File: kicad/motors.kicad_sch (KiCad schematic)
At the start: 33 parts, among them U1 DRV8251A, U15 DRV8251A, U16 DRV8251A, U17 DRV8251A, U2 DRV8251A, U3 DRV8251A

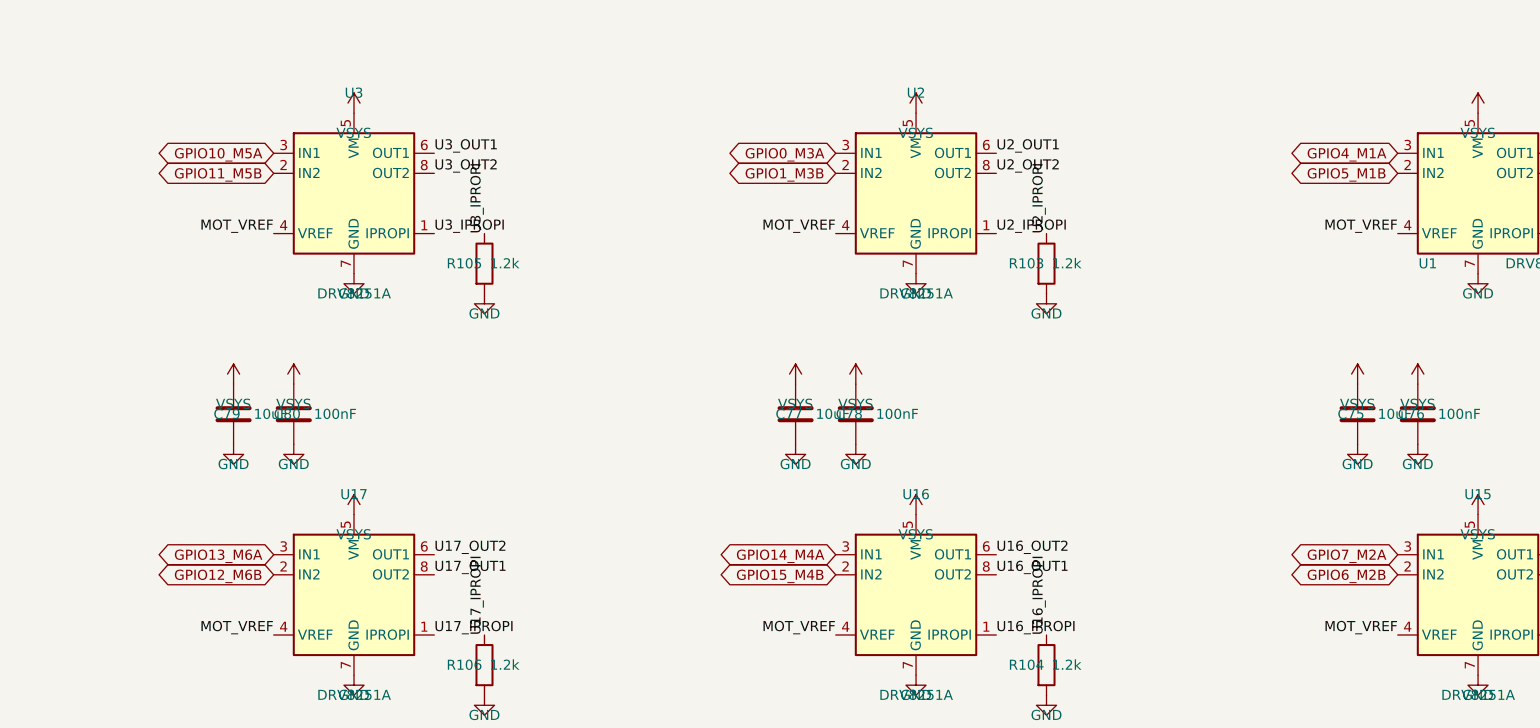
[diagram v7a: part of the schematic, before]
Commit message: Place the brain double-sided at 66.3 x 34 mm, unrouted
- tools/place_double.py rebuilds the placement from scratch: parts on both
  sides, M1-M6 swapped to JST PH S2B-PH-K (C173752), J3 under J4, the
  switches in the bottom-right corner, the USB-C ESD and series resistors
  on the front between J1 and U10.
- Pulls in the 2026-10-20 schematic change (IO5/IO6 off the ADC pins,
  R109/R114 15k USB-A pull-downs).
- Reassigns U10 GPIOs for the new layout, keeping each motor on its own
  PWM slice and IO4-IO6 on slices 1 and 4; USB-A moves to GPIO26/27.
- Adds back-side fiducials FID4-FID6.
- The old partial autoroute is kept in kicad/reference/.

Co-Authored-By: Claude Opus 5.5 <noreply@anthropic.com>
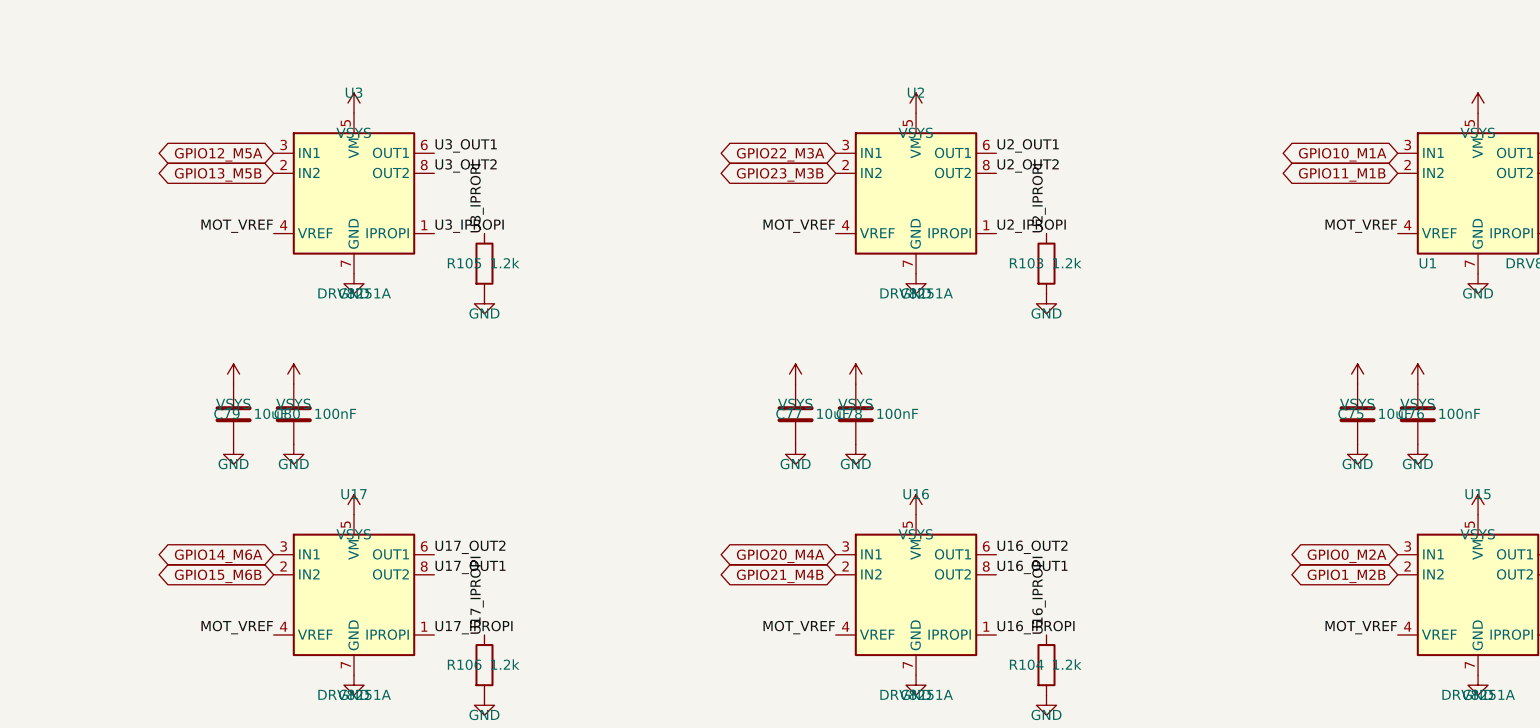
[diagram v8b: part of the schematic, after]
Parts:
- M1, M2, M3, M4, M5, M6: footprint Connector_JST:JST_XH_S2B-XH-A_1x02_P2.50mm_Horizontal -> Connector_JST:JST_PH_S2B-PH-K_1x02_P2.00mm_Horizontal; LCSC Part # C157931 -> C173752; MPN S2B-XH-A(LF)(SN) -> S2B-PH-K-S(LF)(SN)
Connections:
- net GPIO0_M3A renamed GPIO22_M3A
- net GPIO10_M5A renamed GPIO12_M5A
- net GPIO11_M5B renamed GPIO13_M5B
- net GPIO12_M6B renamed GPIO15_M6B
- net GPIO13_M6A renamed GPIO14_M6A
- net GPIO14_M4A renamed GPIO20_M4A
- net GPIO15_M4B renamed GPIO21_M4B
- net GPIO1_M3B renamed GPIO23_M3B
- net GPIO4_M1A renamed GPIO10_M1A
- net GPIO5_M1B renamed GPIO11_M1B
- net GPIO6_M2B renamed GPIO1_M2B
- net GPIO7_M2A renamed GPIO0_M2A
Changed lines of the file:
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@@
 		)
 	)
-	(global_label "GPIO4_M1A"
+	(global_label "GPIO10_M1A"
 		(shape bidirectional)
 		(at 205.74 83.82 180)
@@
 		)
 	)
-	(global_label "GPIO6_M2B"
+	(global_label "GPIO1_M2B"
 		(shape bidirectional)
 		(at 205.74 137.16 180)
@@
 		)
 	)
-	(global_label "GPIO1_M3B"
+	(global_label "GPIO23_M3B"
 		(shape bidirectional)
 		(at 134.62 86.36 180)
@@
 		)
 	)
-	(global_label "GPIO7_M2A"
+	(global_label "GPIO0_M2A"
 		(shape bidirectional)
 		(at 205.74 134.62 180)
@@
 		)
 	)
-	(global_label "GPIO11_M5B"
+	(global_label "GPIO13_M5B"
 		(shape bidirectional)
 		(at 63.5 86.36 180)
@@
 		)
 	)
-	(global_label "GPIO14_M4A"
+	(global_label "GPIO20_M4A"
 		(shape bidirectional)
 		(at 134.62 134.62 180)
@@
 		)
 	)
-	(global_label "GPIO0_M3A"
+	(global_label "GPIO22_M3A"
 		(shape bidirectional)
 		(at 134.62 83.82 180)
@@
 		)
 	)
-	(global_label "GPIO12_M6B"
+	(global_label "GPIO15_M6B"
 		(shape bidirectional)
 		(at 63.5 137.16 180)
@@
 		)
 	)
-	(global_label "GPIO13_M6A"
+	(global_label "GPIO14_M6A"
 		(shape bidirectional)
 		(at 63.5 134.62 180)
@@
 		)
 	)
-	(global_label "GPIO5_M1B"
+	(global_label "GPIO11_M1B"
 		(shape bidirectional)
 		(at 205.74 86.36 180)
@@
 		)
 	)
-	(global_label "GPIO10_M5A"
+	(global_label "GPIO12_M5A"
 		(shape bidirectional)
 		(at 63.5 83.82 180)
@@
 		)
 	)
-	(global_label "GPIO15_M4B"
+	(global_label "GPIO21_M4B"
 		(shape bidirectional)
 		(at 134.62 137.16 180)
@@
 			)
 		)
-		(property "Footprint" "Connector_JST:JST_XH_S2B-XH-A_1x02_P2.50mm_Horizontal"
+		(property "Footprint" "Connector_JST:JST_PH_S2B-PH-K_1x02_P2.00mm_Horizontal"
 			(at 161.29 21.59 0)
 			(hide yes)
@@
 			)
 		)
-		(property "LCSC Part #" "C157931"
+		(property "LCSC Part #" "C173752"
 			(at 182.8801 -142.2401 0)
 			(hide yes)
@@
 			)
 		)
-		(property "MPN" "S2B-XH-A(LF)(SN)"
+		(property "MPN" "S2B-PH-K-S(LF)(SN)"
 			(at 161.29 21.59 0)
 			(hide yes)
@@
 			)
 		)
-		(property "Footprint" "Connector_JST:JST_XH_S2B-XH-A_1x02_P2.50mm_Horizontal"
+		(property "Footprint" "Connector_JST:JST_PH_S2B-PH-K_1x02_P2.00mm_Horizontal"
 			(at 246.38 21.59 0)
 			(hide yes)
@@
 			)
 		)
-		(property "LCSC Part #" "C157931"
+		(property "LCSC Part #" "C173752"
 			(at 224.7899 -224.7901 0)
 			(hide yes)
@@
 			)
 		)
-		(property "MPN" "S2B-XH-A(LF)(SN)"
+		(property "MPN" "S2B-PH-K-S(LF)(SN)"
 			(at 246.38 21.59 0)
 			(hide yes)
@@
 			)
 		)
-		(property "Footprint" "Connector_JST:JST_XH_S2B-XH-A_1x02_P2.50mm_Horizontal"
+		(property "Footprint" "Connector_JST:JST_PH_S2B-PH-K_1x02_P2.00mm_Horizontal"
 			(at 173.99 21.59 0)
 			(hide yes)
@@
 			)
 		)
-		(property "LCSC Part #" "C157931"
+		(property "LCSC Part #" "C173752"
 			(at 152.3999 -152.4001 0)
 			(hide yes)
@@
 			)
 		)
-		(property "MPN" "S2B-XH-A(LF)(SN)"
+		(property "MPN" "S2B-PH-K-S(LF)(SN)"
 			(at 173.99 21.59 0)
 			(hide yes)
@@
 			)
 		)
-		(property "Footprint" "Connector_JST:JST_XH_S2B-XH-A_1x02_P2.50mm_Horizontal"
+		(property "Footprint" "Connector_JST:JST_PH_S2B-PH-K_1x02_P2.00mm_Horizontal"
 			(at 90.17 21.59 0)
 			(hide yes)
@@
 			)
 		)
-		(property "LCSC Part #" "C157931"
+		(property "LCSC Part #" "C173752"
 			(at 111.7601 -71.1201 0)
 			(hide yes)
@@
 			)
 		)
-		(property "MPN" "S2B-XH-A(LF)(SN)"
+		(property "MPN" "S2B-PH-K-S(LF)(SN)"
 			(at 90.17 21.59 0)
 			(hide yes)
@@
 			)
 		)
-		(property "Footprint" "Connector_JST:JST_XH_S2B-XH-A_1x02_P2.50mm_Horizontal"
+		(property "Footprint" "Connector_JST:JST_PH_S2B-PH-K_1x02_P2.00mm_Horizontal"
 			(at 233.68 21.59 0)
 			(hide yes)
@@
 			)
 		)
-		(property "LCSC Part #" "C157931"
+		(property "LCSC Part #" "C173752"
 			(at 255.2701 -214.6301 0)
 			(hide yes)
@@
 			)
 		)
-		(property "MPN" "S2B-XH-A(LF)(SN)"
+		(property "MPN" "S2B-PH-K-S(LF)(SN)"
 			(at 233.68 21.59 0)
 			(hide yes)
@@
 			)
 		)
-		(property "Footprint" "Connector_JST:JST_XH_S2B-XH-A_1x02_P2.50mm_Horizontal"
+		(property "Footprint" "Connector_JST:JST_PH_S2B-PH-K_1x02_P2.00mm_Horizontal"
 			(at 102.87 21.59 0)
 			(hide yes)
@@
 			)
 		)
-		(property "LCSC Part #" "C157931"
+		(property "LCSC Part #" "C173752"
 			(at 81.2799 -81.2801 0)
 			(hide yes)
@@
 			)
 		)
-		(property "MPN" "S2B-XH-A(LF)(SN)"
+		(property "MPN" "S2B-PH-K-S(LF)(SN)"
 			(at 102.87 21.59 0)
 			(hide yes)
